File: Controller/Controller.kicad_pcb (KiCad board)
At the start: 2 copper layers, 64 x 52 mm, 36 parts, among them J101 USB_C_Receptacle, J102 Screw_Terminal_01x02, P101 ESProg_Mating_Header, Q101 BSC0503NSI, SW101 RESET, U101 ESP-12F, U201 LMZM23600V3, U301 STUSB4500QTR

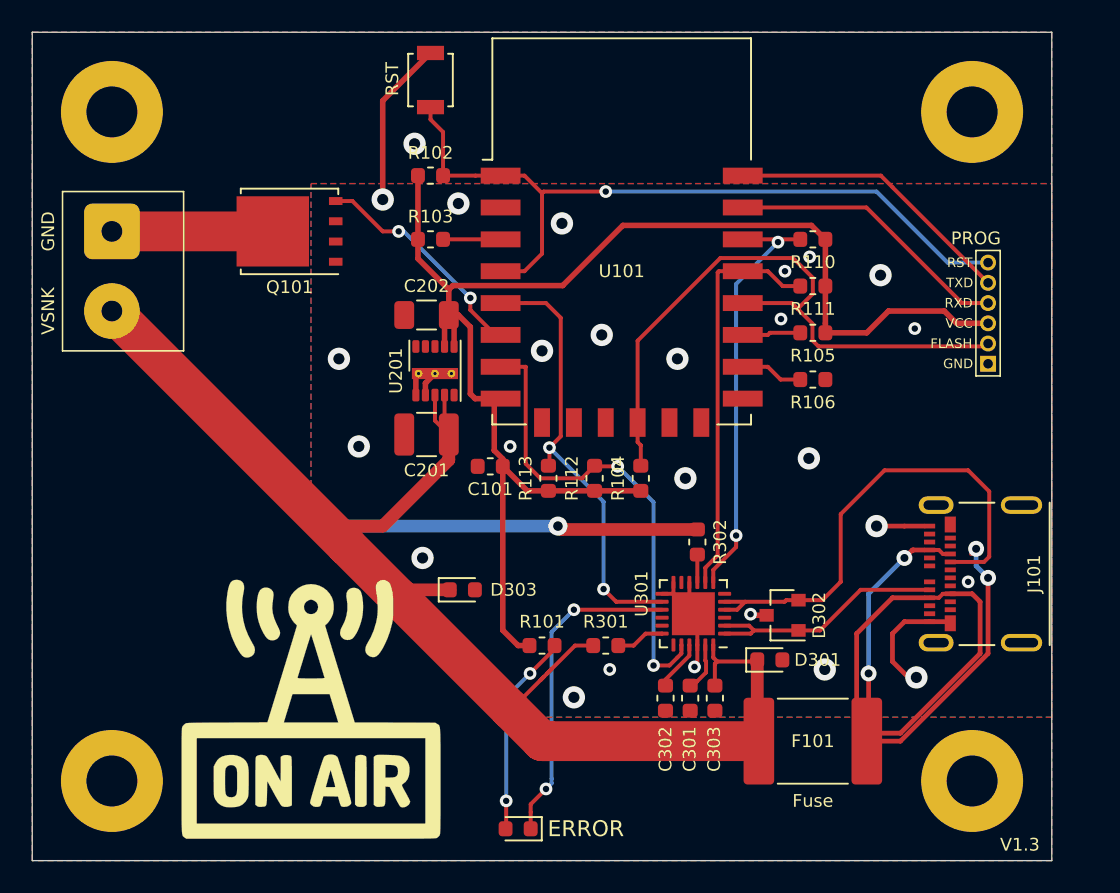
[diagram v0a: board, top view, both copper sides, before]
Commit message: Replaced ESP8266 with ESP32-S2-WROOM
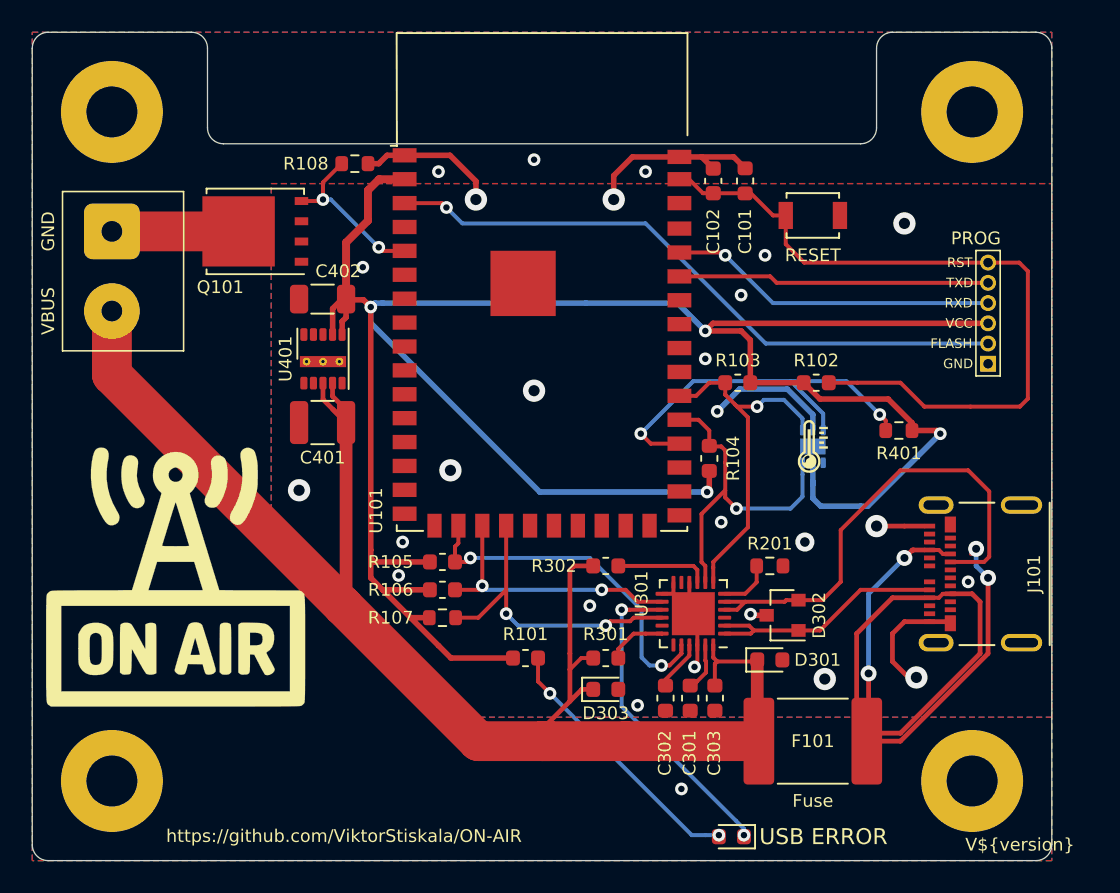
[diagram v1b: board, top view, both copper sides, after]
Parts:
- removed C201: 10uF, Capacitor_SMD:C_1210_3225Metric
- removed C202: 33uF, Capacitor_SMD:C_1206_3216Metric
- removed G***: LOGO, Graphics:ON_AIR
- removed R110, R111, R112, R113: 10K, Resistor_SMD:R_0603_1608Metric
- removed U201: LMZM23600V3, Package_LGA:Texas_SIL0010A_MicroSiP-10-1EP_3.8x3mm_P0.6mm_EP0.7x2.9mm_ThermalVias
- added C102: 0.1uF, Capacitor_SMD:C_0603_1608Metric, F.Cu at (157.8, 74.3)
- added C401: 10uF, Capacitor_SMD:C_1210_3225Metric, F.Cu at (133.2, 89.5)
- added C402: 33uF, Capacitor_SMD:C_1206_3216Metric, F.Cu at (133.2, 81.8)
- added G101: image, Graphics:ON_AIR, F.Cu at (124.0, 99.2)
- added G102: image, Graphics:Temperature, F.Cu at (164.0, 91.0)
- added R107: 10K, Resistor_SMD:R_0603_1608Metric, F.Cu at (140.8, 101.8)
- added R108: 10K, Resistor_SMD:R_0603_1608Metric, F.Cu at (135.2, 73.2)
- added R201: 100K, Resistor_SMD:R_0603_1608Metric, F.Cu at (161.3, 98.5)
- added R401: 10K, Resistor_SMD:R_0603_1608Metric, F.Cu at (169.4, 90.0)
- added U401: LMZM23600V3, Package_LGA:Texas_SIL0010A_MicroSiP-10-1EP_3.8x3mm_P0.6mm_EP0.7x2.9mm_ThermalVias, F.Cu at (133.2, 85.5)
- added U402: TMP117, ViktorStiskala:TMP117_SON65, B.Cu at (164.0, 91.0)
- C101: value 100nF -> 1uF
- U101: value ESP-12F -> ESP32-S2-WROVER; footprint RF_Module:ESP-12E -> RF_Module:ESP32-S2-WROVER
- moved R102 27.5 mm to (164.2, 87.0), turned to 180 degrees
- moved R105 27.3 mm to (140.8, 98.2), turned to 0 degrees
- moved R106 26.7 mm to (140.8, 100.0), turned to 0 degrees
- moved SW101 25.5 mm to (164.0, 76.5), turned to 0 degrees
- moved C101 24.0 mm to (159.8, 74.3), turned to 90 degrees
- moved R103 21.3 mm to (159.3, 87.0), turned to 180 degrees
- moved D101 13.4 mm to (158.9, 115.5)
- moved D303 11.0 mm to (151.0, 106.2)
- moved U101 8.60 mm to (147.0, 84.5)
- moved R302 5.94 mm to (151.0, 98.5), turned to 0 degrees
- moved R104 4.48 mm to (157.5, 91.8)
- moved Q101 2.15 mm to (129.0, 77.5)
- moved R101 1.30 mm to (146.0, 104.3)
- moved R301 0.78 mm to (151.0, 104.3)
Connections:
- net /USB-C PD/GPIO renamed /GPIO
- C101 pad 1: +3V3 -> /ESP_EN
- P101 pad 2: /ESP_GP0 -> /ESP_IO0
- P101 pad 6: /ESP_RST -> /ESP_EN
- R102 pad 1: +3V3 -> /ESP_EN
- R102 pad 2: /ESP_RST -> +3V3
- R103 pad 2: /ESP_EN -> /SCL
- R104 pad 2: /ESP_GP0 -> /SDA
- R105 pad 2: /ESP_GP2 -> /POK2
- R106 pad 1: GND -> +3V3
- R106 pad 2: /ESP_GP15 -> /POK3
- SW101 pad 1: /ESP_RST -> /ESP_EN
- U101 pad 1: /ESP_RST -> GND
- U101 pad 12: /ESP_GP0 -> (no net)
- U101 pad 15: GND -> (no net)
- U101 pad 16: /ESP_GP15 -> (no net)
- U101 pad 17: /ESP_GP2 -> (no net)
- U101 pad 18: /ESP_GP0 -> /POK2
- U101 pad 19: /SDA -> /POK3
- U101 pad 2: (no net) -> +3V3
- U101 pad 20: /SCL -> /VBUS_EN_SNK
- U101 pad 21: /ESP_RX -> (no net)
- U101 pad 22: /ESP_TX -> (no net)
- U101 pad 3: /ESP_EN -> /ESP_IO0
- U101 pad 4: /ESP_RST -> (no net)
- U101 pad 5: /POK3 -> /GP_PWM
- U101 pad 6: /GP_PWM -> (no net)
- U101 pad 7: /POK2 -> (no net)
- U101 pad 8: +3V3 -> (no net)
- U301 pad 16: (no net) -> /VBUS_EN_SNK
- U301 pad 6: (no net) -> /USB-C PD/RST
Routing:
- net +3V3: track 91.4 -> 152.8 mm, vias 0 -> 4
- net /ESP_RST: track 48.0 -> 0.00 mm, vias 1 -> 0
- net /ESP_EN: track 3.61 -> 46.6 mm
- net /ESP_GP0: track 41.2 -> 0.00 mm
- net /ESP_IO0: track 0.00 -> 40.3 mm, vias 0 -> 1
- net VBUS: track 133.3 -> 101.0 mm, vias 1 -> 0
- net /ALERT_TEMP: track 0.00 -> 25.0 mm, vias 0 -> 2
- net /VBUS_EN_SNK: track 0.00 -> 19.7 mm, vias 0 -> 2
- net GND: track 35.7 -> 50.8 mm, vias 25 -> 23
- net /POK3: track 28.1 -> 17.3 mm
- net /POK2: track 30.2 -> 22.1 mm
- net Net-(R302-Pad2): track 1.75 -> 5.89 mm
- net /SDA: track 25.4 -> 21.3 mm, vias 0 -> 1
- net Net-(D101-Pad2): track 12.8 -> 16.8 mm
- net /ESP_GP15: track 3.94 -> 0.00 mm
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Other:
- outline, holes or cut-outs redrawn
- net class 3V3 removed
- net class Default removed
- net class PWR removed
- net class USB_PWR removed
- board text added: "V${version}"
- board text added: "https://github.com/ViktorStiskala/ON-AIR"
- board text removed: "V1.3"

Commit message: V1.3
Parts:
- added R109: 10K, Resistor_SMD:R_0603_1608Metric, F.Cu at (132.5, 93.5)
- added R110: 10K, Resistor_SMD:R_0603_1608Metric, F.Cu at (146.0, 102.0)
- added R111: 10K, Resistor_SMD:R_0603_1608Metric, F.Cu at (169.2, 87.0)
- added SW102: SW_EXT, Connector_PinHeader_2.54mm:PinHeader_1x02_P2.54mm_Vertical, B.Cu at (129.0, 108.1)
- added SW103: SETUP, Button_Switch_SMD:SW_SPST_B3U-1000P, F.Cu at (169.8, 76.5)
- moved G101 2.70 mm to (124.0, 96.5)
- moved P101 1.25 mm to (176.2, 83.3)
- moved R401 0.22 mm to (169.2, 90.0)
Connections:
- U101 pad 15: (no net) -> /SW_EXT
- U101 pad 21: (no net) -> /IO18
- U101 pad 36: (no net) -> /GP_SETUP
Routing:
- net /SW_EXT: track 0.00 -> 30.2 mm, vias 0 -> 2
- net +3V3: track 152.8 -> 177.6 mm, vias 4 -> 6
- net /GP_SETUP: track 0.00 -> 23.0 mm, vias 0 -> 2
- net /IO18: track 0.00 -> 6.25 mm
- net /ESP_IO0: track 40.3 -> 41.8 mm
- net /ESP_RX: track 20.7 -> 22.2 mm
- net /USB_VIN: track 63.4 -> 64.7 mm
- net /ESP_TX: track 19.5 -> 20.8 mm
- net /VBUS_EN_SNK: track 19.7 -> 20.8 mm
- net /ESP_EN: track 46.6 -> 47.7 mm
- net GND: vias 23 -> 28
